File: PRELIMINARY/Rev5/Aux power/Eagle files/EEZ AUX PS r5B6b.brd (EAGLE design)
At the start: 74 x 100 mm, 70 parts, among them IC1 LM25575, IC2 UA78M12DCY, IC3 TPD4E002DRLR, IC4 TPD2E001DZDR, Q1 BTA26-600, Q2 BTA26-600, Q3 IRLL014N, X1 282836-5, X2 09185067324, X3 22-23-2031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

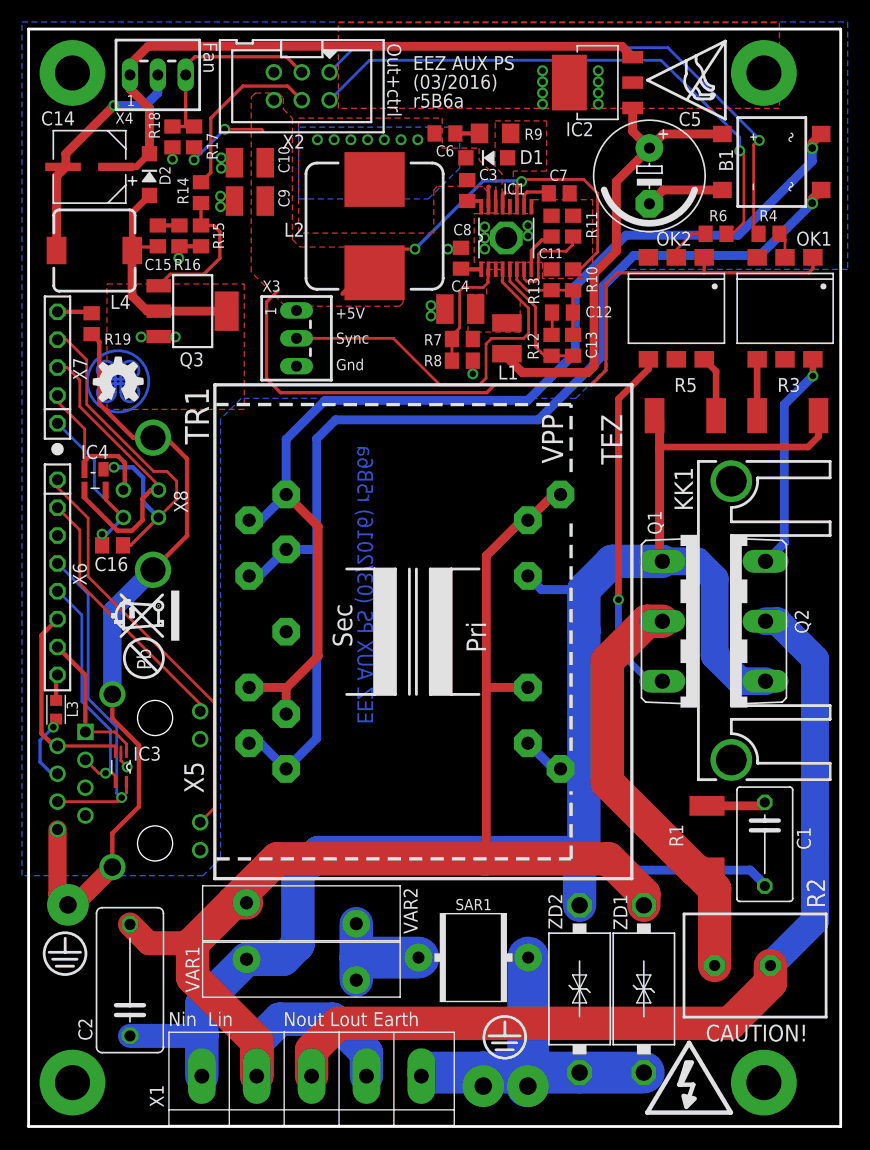
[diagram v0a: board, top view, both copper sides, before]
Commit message: AUX PS r5B6b - added extra mounting tab
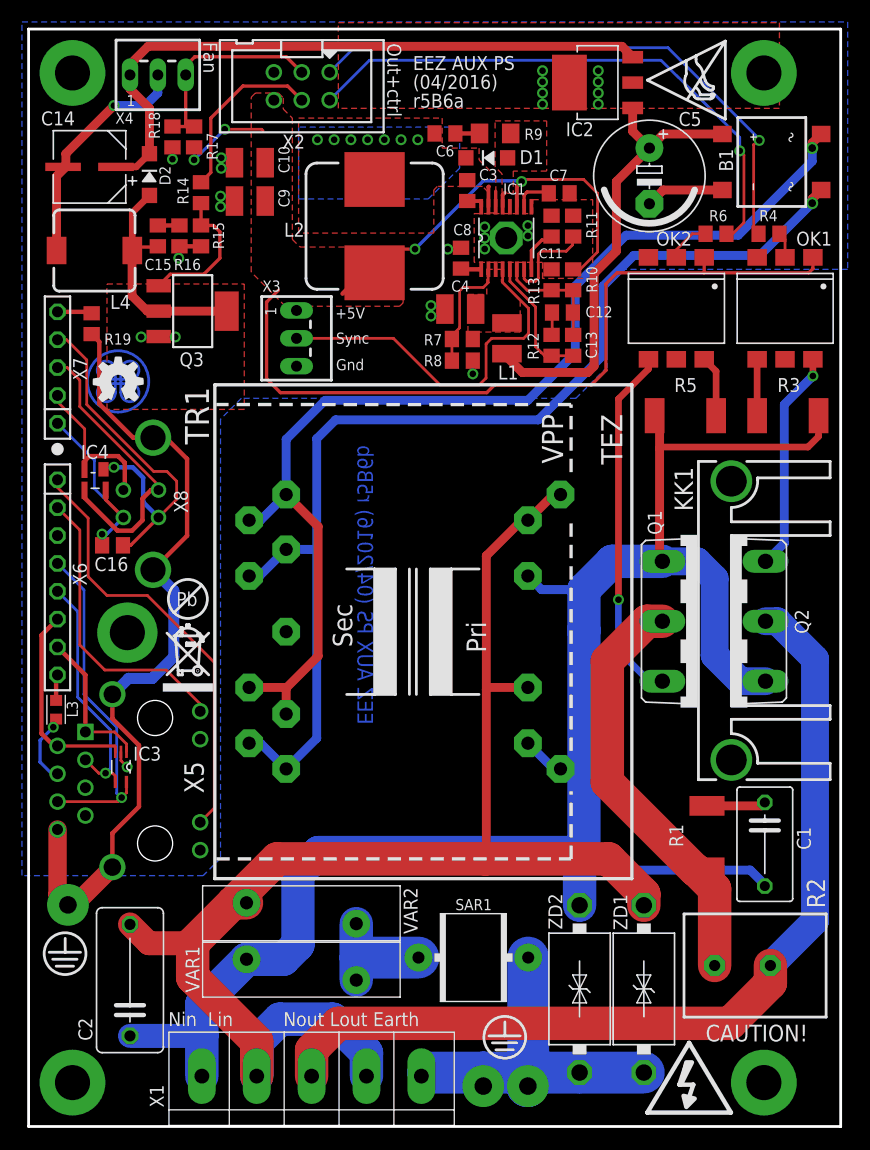
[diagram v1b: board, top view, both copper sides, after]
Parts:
- VAR1, VAR2: value *** -> S20K250
- moved U$3 6.72 mm to (0.51, 48.1), turned to 0 degrees
- moved U$2 4.88 mm to (-1.77, 39.6), turned to 0 degrees
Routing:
- net ETH_ACTLED: track 23.9 -> 27.2 mm
- net AC_EARTH: track 104.2 -> 107.1 mm
- net ETH_LINKLED: track 37.6 -> 39.8 mm
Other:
- board text added: "(04/2016)"
- board text added: "EEZ AUX PS (04/2016) r5B6b"
- board text removed: "(03/2016)"
- board text removed: "EEZ AUX PS (03/2016) r5B6a"
